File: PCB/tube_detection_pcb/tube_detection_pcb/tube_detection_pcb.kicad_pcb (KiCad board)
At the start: 2 copper layers, 73 x 23 mm, 12 parts, among them J1 B6B-XH-A, U1 DM3CQF1003L01, U2 DM3CQF1003L01, U3 DM3CQF1003L01, U4 DM3CQF1003L01, U5 DM3CQF1003L01, U6 SN74HC165N

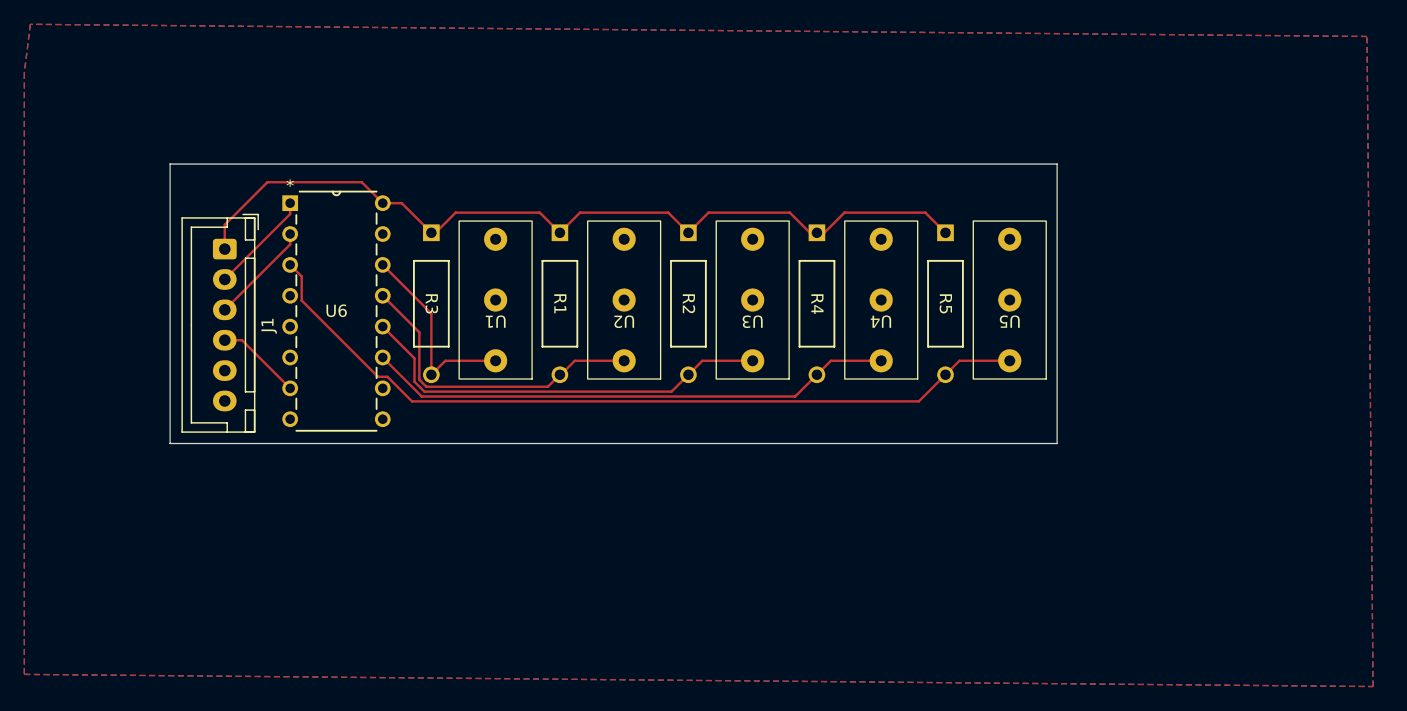
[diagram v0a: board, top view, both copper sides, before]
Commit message: changes to display and tube pcb
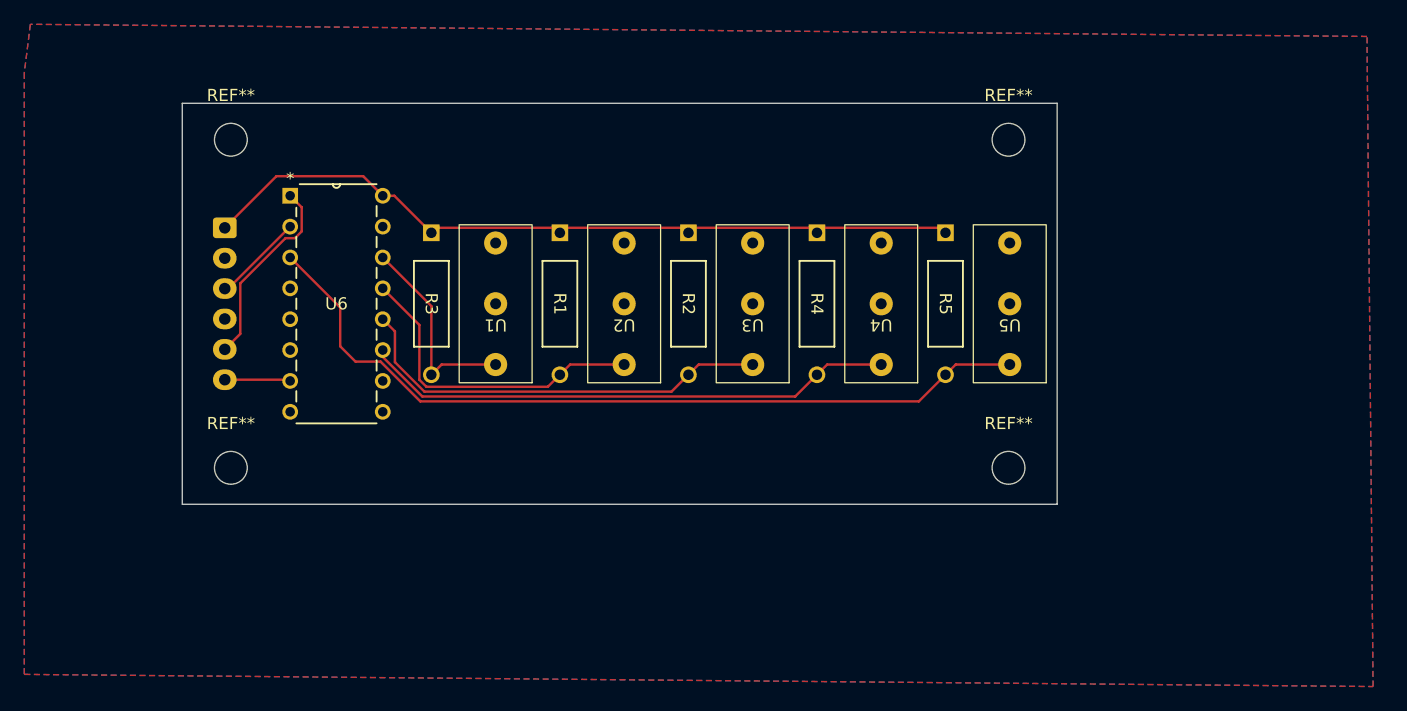
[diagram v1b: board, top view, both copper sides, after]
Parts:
- added REF**: MountingHole_2.7mm, MountingHole:MountingHole_2.7mm, F.Cu at (168.0, 65.0)
- added REF**: MountingHole_2.7mm, MountingHole:MountingHole_2.7mm, F.Cu at (168.0, 38.0)
- added REF**: MountingHole_2.7mm, MountingHole:MountingHole_2.7mm, F.Cu at (104.0, 65.0)
- added REF**: MountingHole_2.7mm, MountingHole:MountingHole_2.7mm, F.Cu at (104.0, 38.0)
- J1: moved to B.Cu
- moved J1 1.75 mm to (103.5, 45.2)
- moved U6 0.61 mm to (116.5, 60.4)
- moved U1 0.31 mm to (125.8, 51.5)
- moved U2 0.31 mm to (136.4, 51.5)
- moved U3 0.31 mm to (146.9, 51.5)
- moved U4 0.31 mm to (157.5, 51.5)
- moved U5 0.31 mm to (168.1, 51.5)
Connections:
- net Net-(U6-CLK) renamed CLK
- J1 pad 2: Net-(U6-SH/*LD) -> GND
- J1 pad 4: Net-(U6-*QH) -> GND
- J1 pad 5: unconnected-(J1-Pad5) -> SH
- J1 pad 6: GND -> QH*
- U6 pad 1: Net-(U6-SH/*LD) -> SH
- U6 pad 7: Net-(U6-*QH) -> QH*
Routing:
- net SH: track 0.00 -> 16.1 mm
- net Net-(U6-SH/*LD): track 8.90 -> 0.00 mm
- net Net-(U6-*QH): track 7.02 -> 0.00 mm
- net +3V3: track 70.0 -> 64.4 mm
- net QH*: track 0.00 -> 5.42 mm
- net CLK: track 8.81 -> 7.49 mm
- net Net-(U5-C): track 66.4 -> 67.2 mm
- net GND: track 0.00 -> 0.52 mm
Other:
- board size 73 x 23 mm -> 72 x 33 mm

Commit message: pcb silkscreens mostly
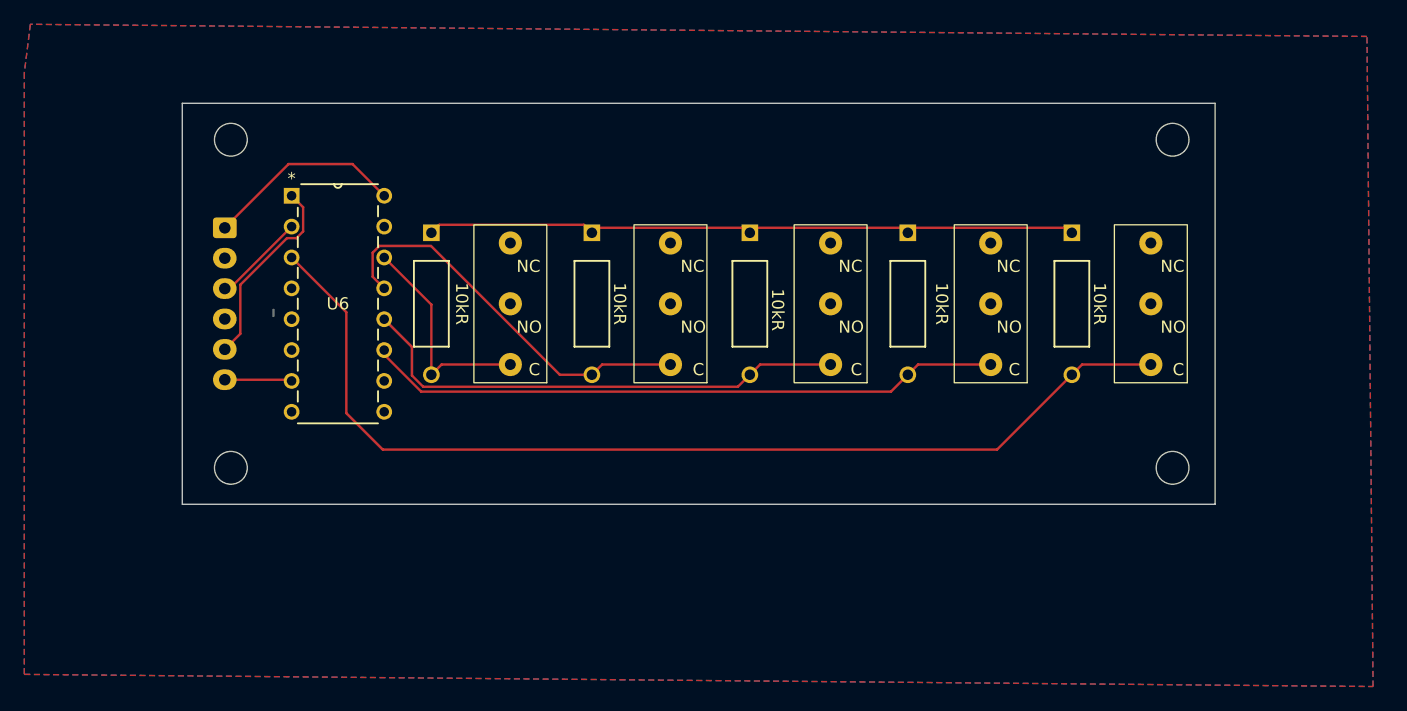
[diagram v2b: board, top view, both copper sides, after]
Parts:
- moved REF** 13.5 mm to (181.5, 65.0)
- moved REF** 13.5 mm to (181.5, 38.0)
- moved U5 11.6 mm to (179.7, 51.5)
- moved 10kR 10.4 mm to (173.2, 45.7)
- moved U4 9.01 mm to (166.5, 51.5)
- moved 10kR 7.48 mm to (159.7, 45.7)
- moved U3 6.41 mm to (153.4, 51.5)
- moved 10kR 5.06 mm to (146.7, 45.7)
- moved U2 3.81 mm to (140.2, 51.5)
- moved 10kR 2.63 mm to (133.7, 45.7)
- moved U1 1.21 mm to (127.0, 51.5)
- moved U6 0.12 mm to (116.6, 60.4)
- renumbered R1 to 10kR, R2 to 10kR, R4 to 10kR, R5 to 10kR, R3 to 10kR
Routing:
- net Net-(U5-C): track 67.2 -> 85.0 mm
- net Net-(U4-C): track 44.0 -> 52.5 mm
- net +3V3: track 64.4 -> 70.7 mm
- net Net-(U2-C): track 26.6 -> 32.8 mm
- net Net-(U3-C): track 35.3 -> 41.2 mm
- net Net-(U1-C): track 16.9 -> 18.1 mm
- net GND: track 0.52 -> 0.00 mm
- net (no net): track 0.00 -> 0.50 mm
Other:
- board size 72 x 33 mm -> 85 x 33 mm
- board text added: "C"
- board text added: "NC"
- board text added: "NO"

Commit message: pcb stuff i forget
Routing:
- net Net-(U5-C): track 85.0 -> 6.85 mm
- net +3V3: track 70.7 -> 18.6 mm
- net Net-(U4-C): track 52.5 -> 7.17 mm
- net Net-(U3-C): track 41.2 -> 6.99 mm
- net Net-(U2-C): track 32.8 -> 6.82 mm
- net Net-(U1-C): track 18.1 -> 6.85 mm
- net SH: track 16.2 -> 17.7 mm
- net CLK: track 7.61 -> 8.74 mm
- net (no net): track 0.50 -> 0.00 mm
- removed copper zone on F.Cu, net GND

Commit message: pcb repin
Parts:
- moved U6 1.61 mm to (116.6, 62.0)
- renumbered 10kR to R1, 10kR to R2, 10kR to R3, 10kR to R4, 10kR to R5
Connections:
- J1 pad 3: CLK -> SH
- J1 pad 5: SH -> CLK
- U6 pad 10: unconnected-(U6-SER-Pad10) -> GND
- U6 pad 15: unconnected-(U6-CLKINH-Pad15) -> GND
- U6 pad 4: unconnected-(U6-F-Pad4) -> GND
- U6 pad 5: unconnected-(U6-G-Pad5) -> GND
- U6 pad 6: unconnected-(U6-H-Pad6) -> GND
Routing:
- net Net-(U5-C): track 6.85 -> 79.9 mm
- net Net-(U4-C): track 7.17 -> 53.1 mm
- net Net-(U3-C): track 6.99 -> 42.1 mm
- net Net-(U2-C): track 6.82 -> 30.2 mm
- net Net-(U1-C): track 6.85 -> 16.5 mm
- net SH: track 17.7 -> 8.31 mm
- net +3V3: track 18.6 -> 16.2 mm
- net CLK: track 8.74 -> 10.8 mm
- net QH*: track 5.54 -> 6.21 mm

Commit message: PCB updates
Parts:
- moved R3 2.59 mm to (123.0, 45.0)
- moved R1 2.34 mm to (136.0, 45.2)
- moved R2 2.34 mm to (149.0, 45.2)
- moved R4 2.34 mm to (162.0, 45.2)
- moved U1 2.00 mm to (129.0, 51.5)
- moved R5 1.86 mm to (175.0, 45.2)
- moved U2 1.82 mm to (142.0, 51.5)
- moved U3 1.64 mm to (155.0, 51.5)
- moved U4 1.47 mm to (168.0, 51.5)
- moved U6 1.40 mm to (118.0, 61.8)
- moved U5 1.29 mm to (181.0, 51.5)
- moved REF** 0.50 mm to (182.0, 65.0)
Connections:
- J1 pad 4: GND -> CLK
- J1 pad 5: CLK -> CSn
- U1 pad 2: GND -> Net-(U1-NO)
- U1 pad 3: unconnected-(U1-NC-Pad3) -> GND
- U2 pad 2: GND -> Net-(U2-NO)
- U2 pad 3: unconnected-(U2-NC-Pad3) -> GND
- U3 pad 2: GND -> Net-(U3-NO)
- U3 pad 3: unconnected-(U3-NC-Pad3) -> GND
- U4 pad 2: GND -> Net-(U4-NO)
- U4 pad 3: unconnected-(U4-NC-Pad3) -> GND
- U5 pad 2: GND -> Net-(U5-NO)
- U5 pad 3: unconnected-(U5-NC-Pad3) -> GND
- U6 pad 11: Net-(U4-C) -> Net-(U4-NO)
- U6 pad 12: Net-(U3-C) -> Net-(U3-NO)
- U6 pad 13: Net-(U2-C) -> Net-(U2-NO)
- U6 pad 14: Net-(U1-C) -> Net-(U1-NO)
- U6 pad 15: GND -> CSn
- U6 pad 3: Net-(U5-C) -> Net-(U5-NO)
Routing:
- net Net-(U5-C): track 79.9 -> 6.14 mm
- net Net-(U5-NO): track 0.00 -> 72.4 mm
- net +3V3: track 16.2 -> 78.9 mm
- net Net-(U4-NO): track 0.00 -> 52.2 mm
- net Net-(U4-C): track 53.1 -> 6.14 mm
- net Net-(U3-NO): track 0.00 -> 38.1 mm
- net Net-(U3-C): track 42.1 -> 6.14 mm
- net Net-(U2-NO): track 0.00 -> 25.0 mm
- net Net-(U2-C): track 30.2 -> 6.14 mm
- net CSn: track 0.00 -> 18.5 mm
- net Net-(U1-NO): track 0.00 -> 12.0 mm
- net Net-(U1-C): track 16.5 -> 6.08 mm
- net CLK: track 10.8 -> 9.45 mm
- net QH*: track 6.21 -> 7.50 mm
- net SH: track 8.31 -> 9.47 mm
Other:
- board text added: "10kR * 5"

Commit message: pcb finishing touches
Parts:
- removed the REF** at (182.0, 65.0)
- removed the REF** at (181.5, 38.0)
- removed the REF** at (104.0, 65.0)
- removed the REF** at (104.0, 38.0)
- added REF**: MountingHole_3.2mm_M3, MountingHole:MountingHole_3.2mm_M3, F.Cu at (104.0, 64.2)
- added REF**: MountingHole_3.2mm_M3, MountingHole:MountingHole_3.2mm_M3, F.Cu at (195.0, 38.5)
- added REF**: MountingHole_3.2mm_M3, MountingHole:MountingHole_3.2mm_M3, F.Cu at (104.0, 38.5)
- added REF**: MountingHole_3.2mm_M3, MountingHole:MountingHole_3.2mm_M3, F.Cu at (195.0, 64.2)
- moved J1 12.6 mm to (104.8, 57.8), turned to 90 degrees
- moved R5 8.00 mm to (183.0, 45.2)
- moved U5 8.00 mm to (189.0, 51.5)
- moved R4 6.00 mm to (168.0, 45.2)
- moved U4 6.00 mm to (174.0, 51.5)
- moved R2 4.00 mm to (153.0, 45.2)
- moved U3 4.00 mm to (159.0, 51.5)
- moved R1 2.00 mm to (138.0, 45.2)
- moved U2 2.00 mm to (144.0, 51.5)
- moved U6 1.54 mm to (118.0, 60.2)
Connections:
- J1 pad 3: SH -> QH*
- J1 pad 5: CSn -> SH
- J1 pad 6: QH* -> CSn
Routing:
- net +3V3: track 78.9 -> 103.1 mm
- net Net-(U5-NO): track 72.4 -> 87.7 mm
- net Net-(U4-NO): track 52.2 -> 57.5 mm
- net Net-(U3-NO): track 38.1 -> 42.4 mm
- net Net-(U2-NO): track 25.0 -> 27.6 mm
- net CSn: track 18.5 -> 16.2 mm
- net SH: track 9.47 -> 7.82 mm
- net CLK: track 9.45 -> 7.80 mm
- net Net-(U1-NO): track 12.0 -> 12.6 mm
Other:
- board size 85 x 33 mm -> 98.8 x 33 mm
- board text removed: "NO"
